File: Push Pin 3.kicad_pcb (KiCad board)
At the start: 2 copper layers, 92 x 75.9 mm, 34 parts, among them J1 Screw_Terminal_01x02, J2 Screw_Terminal_01x02, J3 Screw_Terminal_01x02, J4 Screw_Terminal_01x02, J5 Screw_Terminal_01x02, J6 Screw_Terminal_01x02, J7 Screw_Terminal_01x02, Q1 NTR4101PT1G, Q2 NTR4101PT1G, Q3 NTR4101PT1G, SW4 SW_DPDT_x2, SW5 SW_DPDT_x2, SW6 SW_DPDT_x2, U2 LDO_4v2-MIC5209-4.2YS-TR

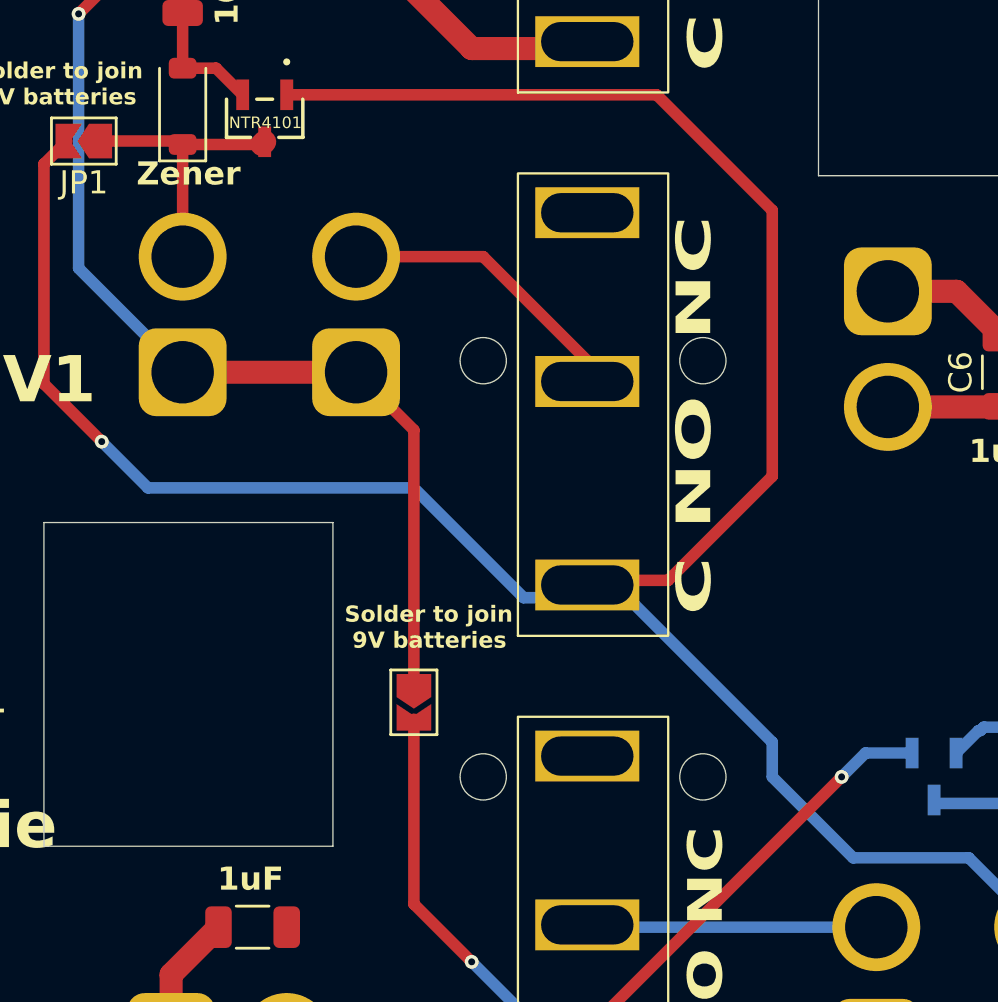
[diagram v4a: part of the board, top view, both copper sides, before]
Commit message: Modifications positions switch et xt30
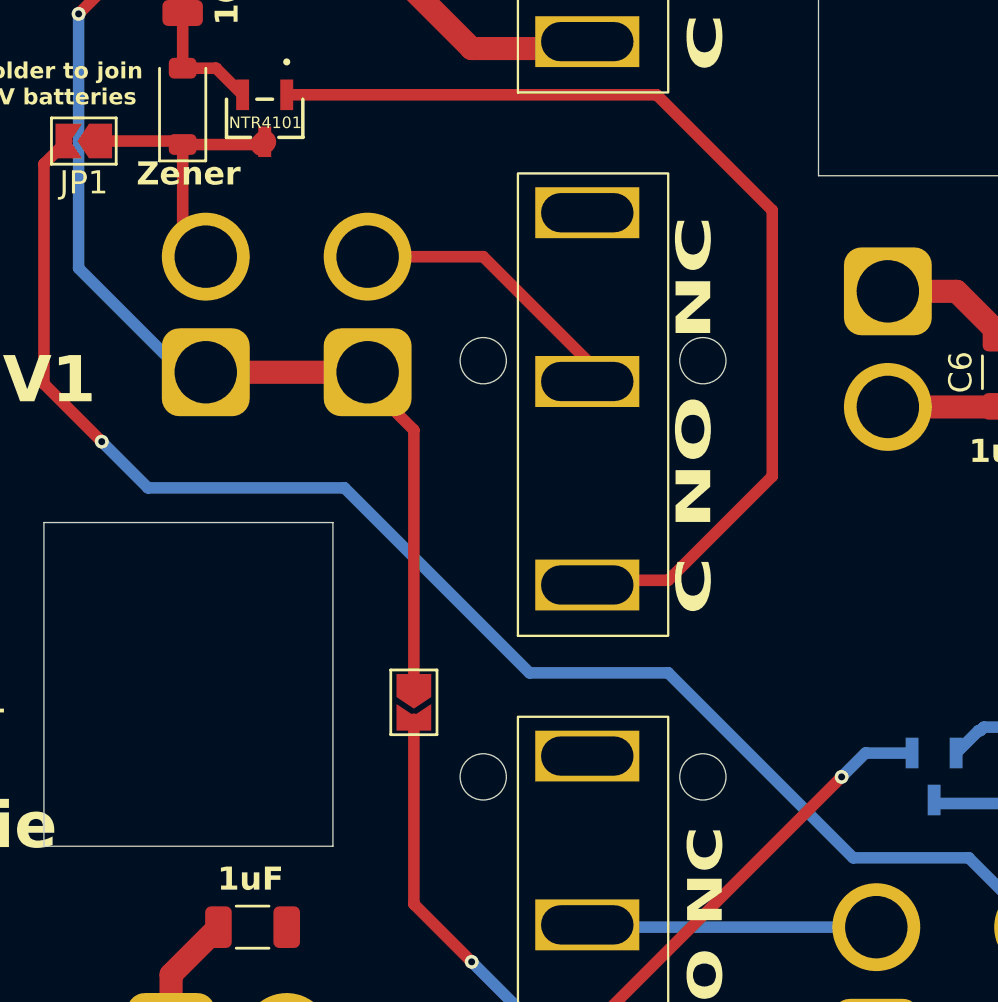
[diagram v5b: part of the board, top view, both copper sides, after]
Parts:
- moved J3 1.00 mm to (133.5, 108.5)
- moved Batt_7v2 0.50 mm to (140.5, 108.5)
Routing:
- net 9V: track 74.4 -> 73.6 mm
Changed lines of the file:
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@@
 	(footprint "Connector_AMASS:AMASS_XT30U-M_1x02_P5.0mm_Vertical"
 		(layer "B.Cu")
-		(at 140 108.5 90)
+		(at 140.5 108.5 90)
 		(descr "Connector XT30 Vertical Cable Male, https://www.tme.eu/Document/7d9d972ae3468777f69ec2ee99897652/XT30U-M.pdf")
 		(tags "RC Connector XT30")
@@
 	(footprint "Connector_AMASS:AMASS_XT30U-M_1x02_P5.0mm_Vertical"
 		(layer "B.Cu")
-		(at 132.5 108.5 90)
+		(at 133.5 108.5 90)
 		(descr "Connector XT30 Vertical Cable Male, https://www.tme.eu/Document/7d9d972ae3468777f69ec2ee99897652/XT30U-M.pdf")
 		(tags "RC Connector XT30")
@@
 		)
 	)
-	(gr_text "Solder to join \n 9V batteries"
-		(at 139.5 120.5 0)
-		(layer "F.SilkS")
-		(effects
-			(font
-				(size 0.7 0.7)
-				(thickness 0.175)
-				(bold yes)
-			)
-			(justify left bottom)
-		)
-	)
 	(gr_text "NTR4101"
 		(at 134.5 98 0)
@@
 	)
 	(segment
-		(start 129 111.5)
-		(end 131 113.5)
-		(width 0.5)
-		(layer "B.Cu")
-		(net 14)
-	)
-	(segment
 		(start 165.15 127.15)
 		(end 165 127)
@@
 	)
 	(segment
-		(start 158 124.5)
-		(end 158 126)
-		(width 0.5)
-		(layer "B.Cu")
-		(net 14)
-	)
-	(segment
-		(start 161.5 129.5)
-		(end 166.5 129.5)
+		(start 166.5 129.5)
+		(end 169.5 132.5)
 		(width 0.5)
 		(layer "B.Cu")
@@
 	)
 	(segment
-		(start 169.5 127.15)
-		(end 165.15 127.15)
+		(start 129 111.5)
+		(end 131 113.5)
 		(width 0.5)
 		(layer "B.Cu")
@@
 	)
 	(segment
-		(start 166.5 129.5)
-		(end 169.5 132.5)
+		(start 161.5 129.5)
+		(end 166.5 129.5)
 		(width 0.5)
 		(layer "B.Cu")
@@
 	)
 	(segment
-		(start 151.75 118.25)
-		(end 158 124.5)
+		(start 153.5 121.5)
+		(end 161.5 129.5)
 		(width 0.5)
 		(layer "B.Cu")
@@
 	)
 	(segment
-		(start 151.75 118.25)
-		(end 147.25 118.25)
+		(start 169.5 127.15)
+		(end 165.15 127.15)
 		(width 0.5)
 		(layer "B.Cu")
@@
 	)
 	(segment
-		(start 169.5 127.15)
-		(end 169.5 132.5)
+		(start 147.5 121.5)
+		(end 153.5 121.5)
 		(width 0.5)
 		(layer "B.Cu")
@@
 	)
 	(segment
-		(start 158 126)
-		(end 161.5 129.5)
+		(start 131 113.5)
+		(end 139.5 113.5)
 		(width 0.5)
 		(layer "B.Cu")
@@
 	)
 	(segment
-		(start 142.5 113.5)
-		(end 131 113.5)
+		(start 139.5 113.5)
+		(end 147.5 121.5)
 		(width 0.5)
 		(layer "B.Cu")
@@
 	)
 	(segment
-		(start 147.25 118.25)
-		(end 142.5 113.5)
+		(start 169.5 127.15)
+		(end 169.5 132.5)
 		(width 0.5)
 		(layer "B.Cu")
@@
 	)
 	(segment
-		(start 132.5 103.5)
-		(end 132.5 98.65)
+		(start 132.5 98.65)
+		(end 135.9295 98.65)
 		(width 0.5)
 		(layer "F.Cu")
@@
 	)
 	(segment
-		(start 132.5 98.65)
-		(end 135.9295 98.65)
+		(start 133.5 103.5)
+		(end 132.5 102.5)
 		(width 0.5)
 		(layer "F.Cu")
@@
 		(width 0.5)
 		(layer "F.Cu")
+		(net 15)
+	)
+	(segment
+		(start 132.5 102.5)
+		(end 132.5 98.65)
+		(width 0.5)
+		(layer "F.Cu")

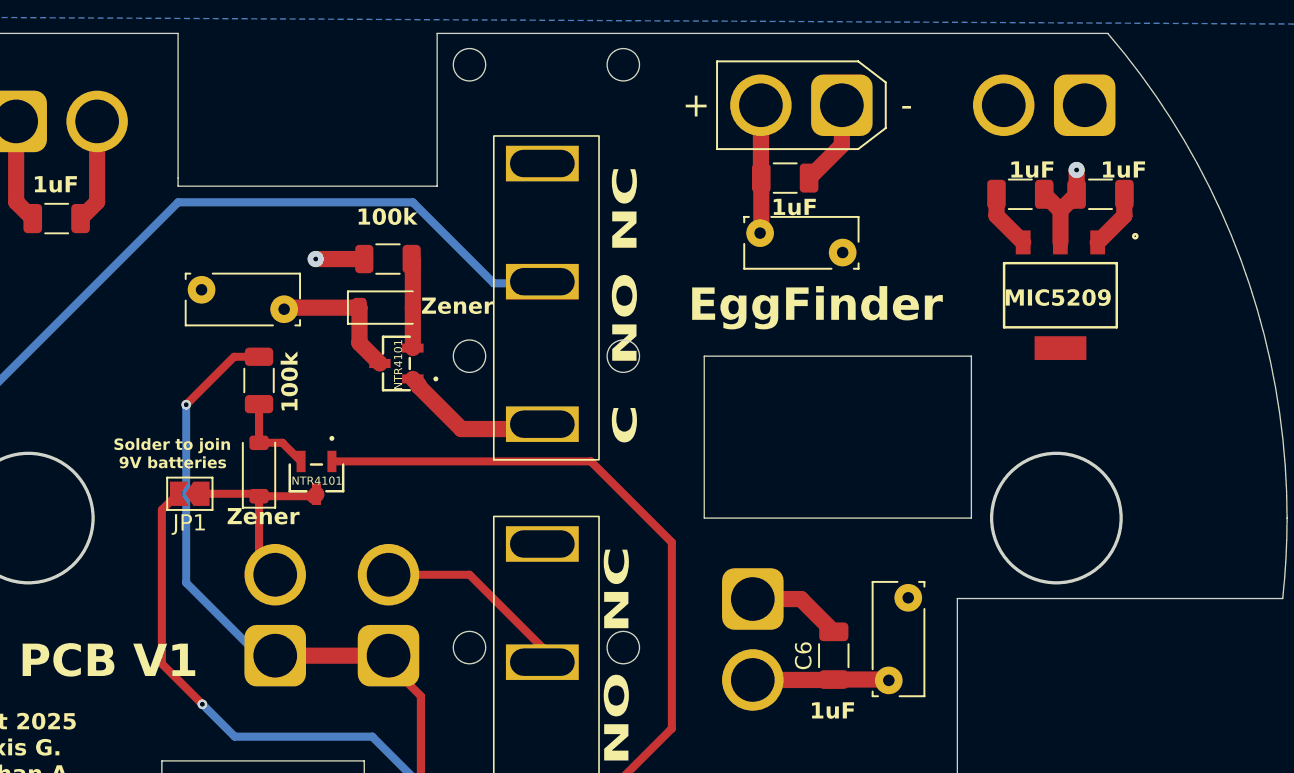
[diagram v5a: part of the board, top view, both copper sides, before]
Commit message: Modifs silkscreen + odb1 3v7 connecteur
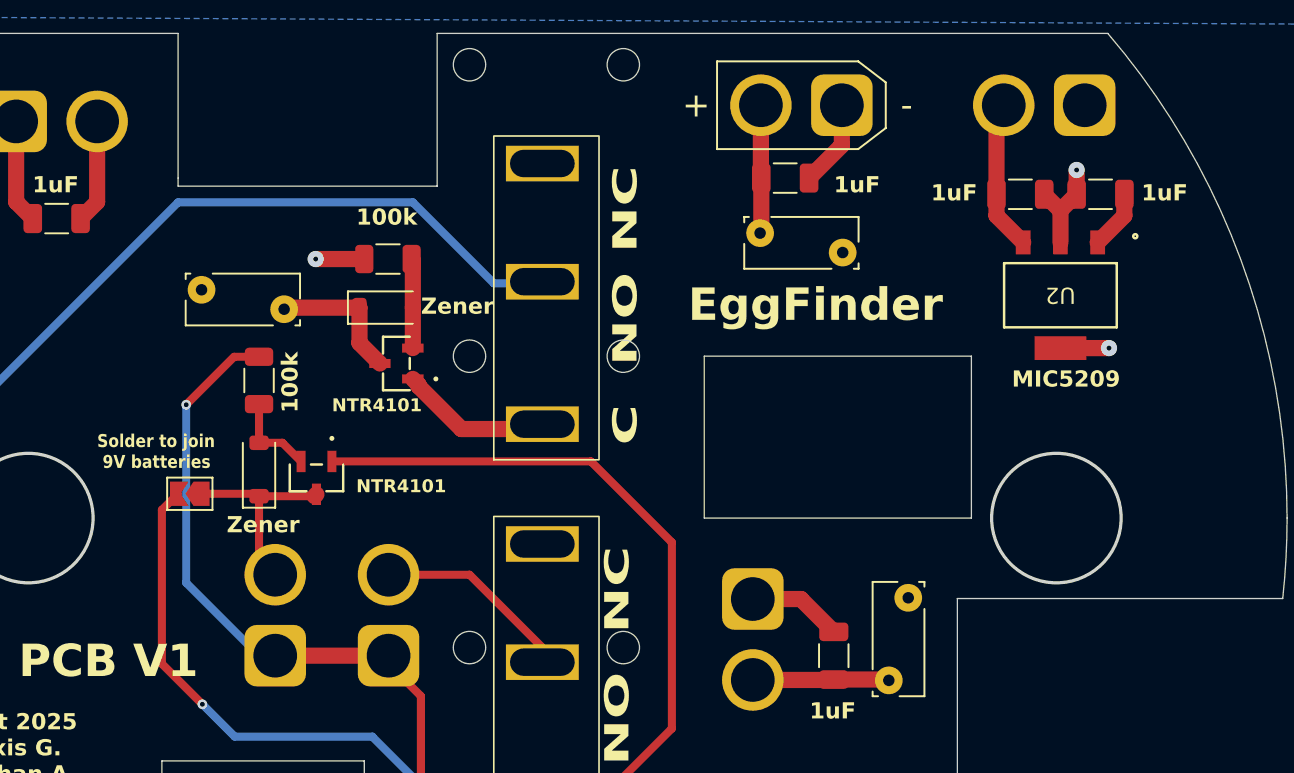
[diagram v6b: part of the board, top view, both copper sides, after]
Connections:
- C5 pad 1: Net-(U2-OUT) -> Net-(J7-Pin_2)
- J7 pad 1: unconnected-(J7-Pin_1-Pad1) -> GND
- J7 pad 2: unconnected-(J7-Pin_2-Pad2) -> Net-(J7-Pin_2)
- U2 pad 3: Net-(U2-OUT) -> Net-(J7-Pin_2)
- U2 pad 4: unconnected-(U2-Pad4) -> GND
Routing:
- net Net-(J7-Pin_2): track 0.00 -> 9.34 mm
- net Net-(U2-OUT): track 3.66 -> 0.00 mm
- net GND: track 31.5 -> 34.5 mm, vias 2 -> 3

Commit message: Plus beau
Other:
- board text added: "+"
- board text added: "-"
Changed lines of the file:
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@@
 		)
 		(fp_text user "+"
-			(at 14.5 -2.595 90)
+			(at 10 -0.5 90)
 			(layer "B.SilkS")
 			(effects
@@
 		)
 	)
+	(gr_text "-"
+		(at 139.5 113 0)
+		(layer "B.SilkS")
+		(effects
+			(font
+				(size 1.5 1.5)
+				(thickness 0.15)
+			)
+			(justify left bottom)
+		)
+	)
 	(gr_text "ODB1\n3v7\n"
 		(at 185.4798 84.2549 0)
@@
 		)
 	)
+	(gr_text "+"
+		(at 168.5 129.5 0)
+		(layer "B.SilkS")
+		(effects
+			(font
+				(size 1.5 1.5)
+				(thickness 0.15)
+			)
+			(justify left bottom)
+		)
+	)
 	(gr_text "Easymini"
 		(at 137.5 114.5 0)
@@
 	)
 	(gr_text "9V"
-		(at 142 114 0)
+		(at 146 113 0)
 		(layer "B.SilkS")
 		(effects
@@
 		)
 	)
+	(gr_text "+"
+		(at 140 100 0)
+		(layer "B.SilkS")
+		(effects
+			(font
+				(size 1.5 1.5)
+				(thickness 0.15)
+			)
+			(justify left bottom)
+		)
+	)
+	(gr_text "+"
+		(at 132.5 100 0)
+		(layer "B.SilkS")
+		(effects
+			(font
+				(size 1.5 1.5)
+				(thickness 0.15)
+			)
+			(justify left bottom)
+		)
+	)

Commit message: touch up
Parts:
- moved J3 0.50 mm to (134.0, 108.5)
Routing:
- net Net-(DZ3-K): track 12.5 -> 13.2 mm
- net Net-(Batt_7v2-Pin_1): track 45.2 -> 45.7 mm
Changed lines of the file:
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@@
 	(footprint "Connector_AMASS:AMASS_XT30U-M_1x02_P5.0mm_Vertical"
 		(layer "B.Cu")
-		(at 133.5 108.5 90)
+		(at 134 108.5 90)
 		(descr "Connector XT30 Vertical Cable Male, https://www.tme.eu/Document/7d9d972ae3468777f69ec2ee99897652/XT30U-M.pdf")
 		(tags "RC Connector XT30")
@@
 	)
 	(segment
-		(start 132.5 108.5)
-		(end 140 108.5)
+		(start 134 108.5)
+		(end 140.5 108.5)
 		(width 1)
 		(layer "F.Cu")
@@
 	)
 	(segment
+		(start 132.5 108.5)
+		(end 134 108.5)
+		(width 0.5)
+		(layer "B.Cu")
+		(net 6)
+	)
+	(segment
 		(start 128 104)
 		(end 132.5 108.5)
@@
 	)
 	(segment
-		(start 133.5 103.5)
-		(end 132.5 102.5)
+		(start 132.5 102)
+		(end 132.5 98.65)
 		(width 0.5)
 		(layer "F.Cu")
@@
 	)
 	(segment
-		(start 132.35 98.5)
-		(end 132.5 98.65)
+		(start 134 103.5)
+		(end 132.5 102)
 		(width 0.5)
 		(layer "F.Cu")
@@
 	)
 	(segment
-		(start 128.95 98.5)
-		(end 132.35 98.5)
+		(start 133.5 103.5)
+		(end 134 103.5)
 		(width 0.5)
 		(layer "F.Cu")
@@
 	)
 	(segment
-		(start 132.5 102.5)
+		(start 132.35 98.5)
 		(end 132.5 98.65)
 		(width 0.5)
 		(layer "F.Cu")
+		(net 14)
+	)
+	(segment
+		(start 128.95 98.5)
+		(end 132.35 98.5)
+		(width 0.5)
+		(layer "F.Cu")
